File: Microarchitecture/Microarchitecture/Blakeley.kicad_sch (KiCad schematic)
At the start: 13 parts

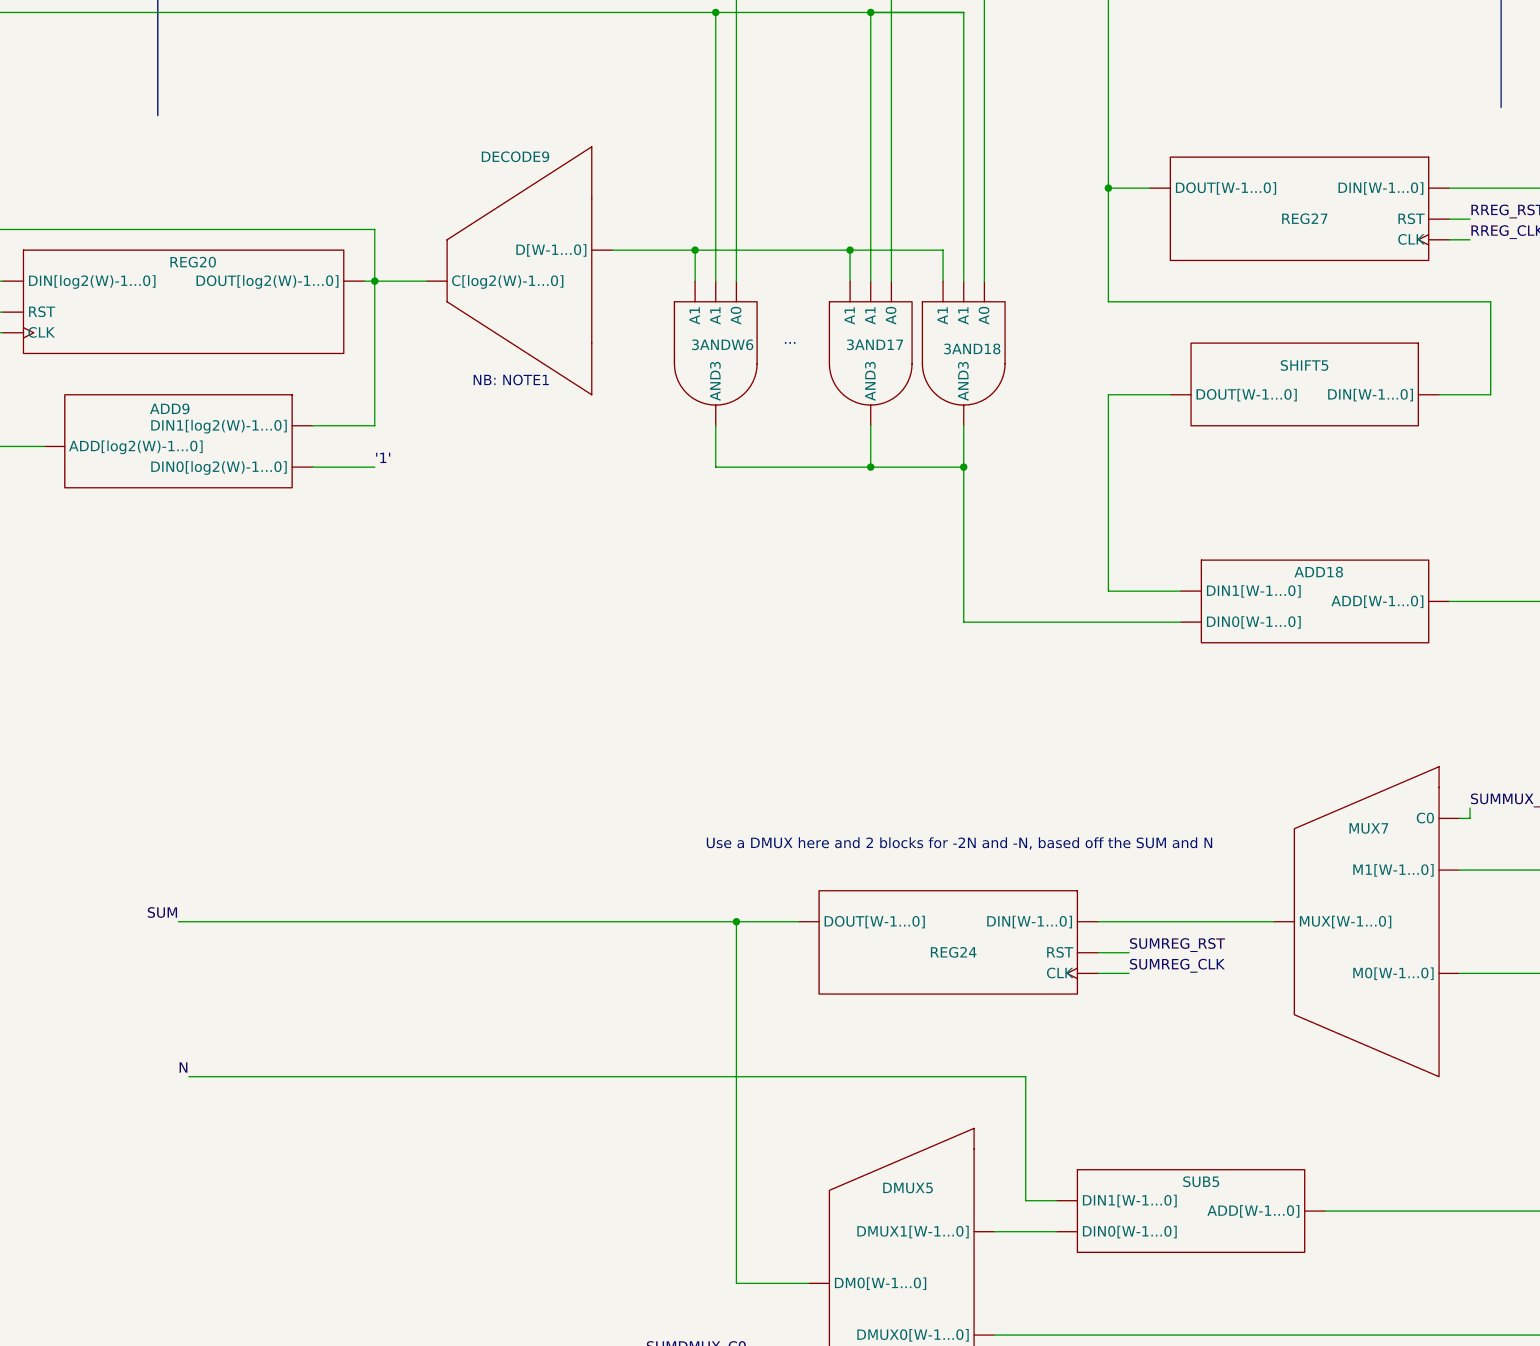
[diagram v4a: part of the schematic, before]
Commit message: Added comments, 16 to 8 stage pipeline
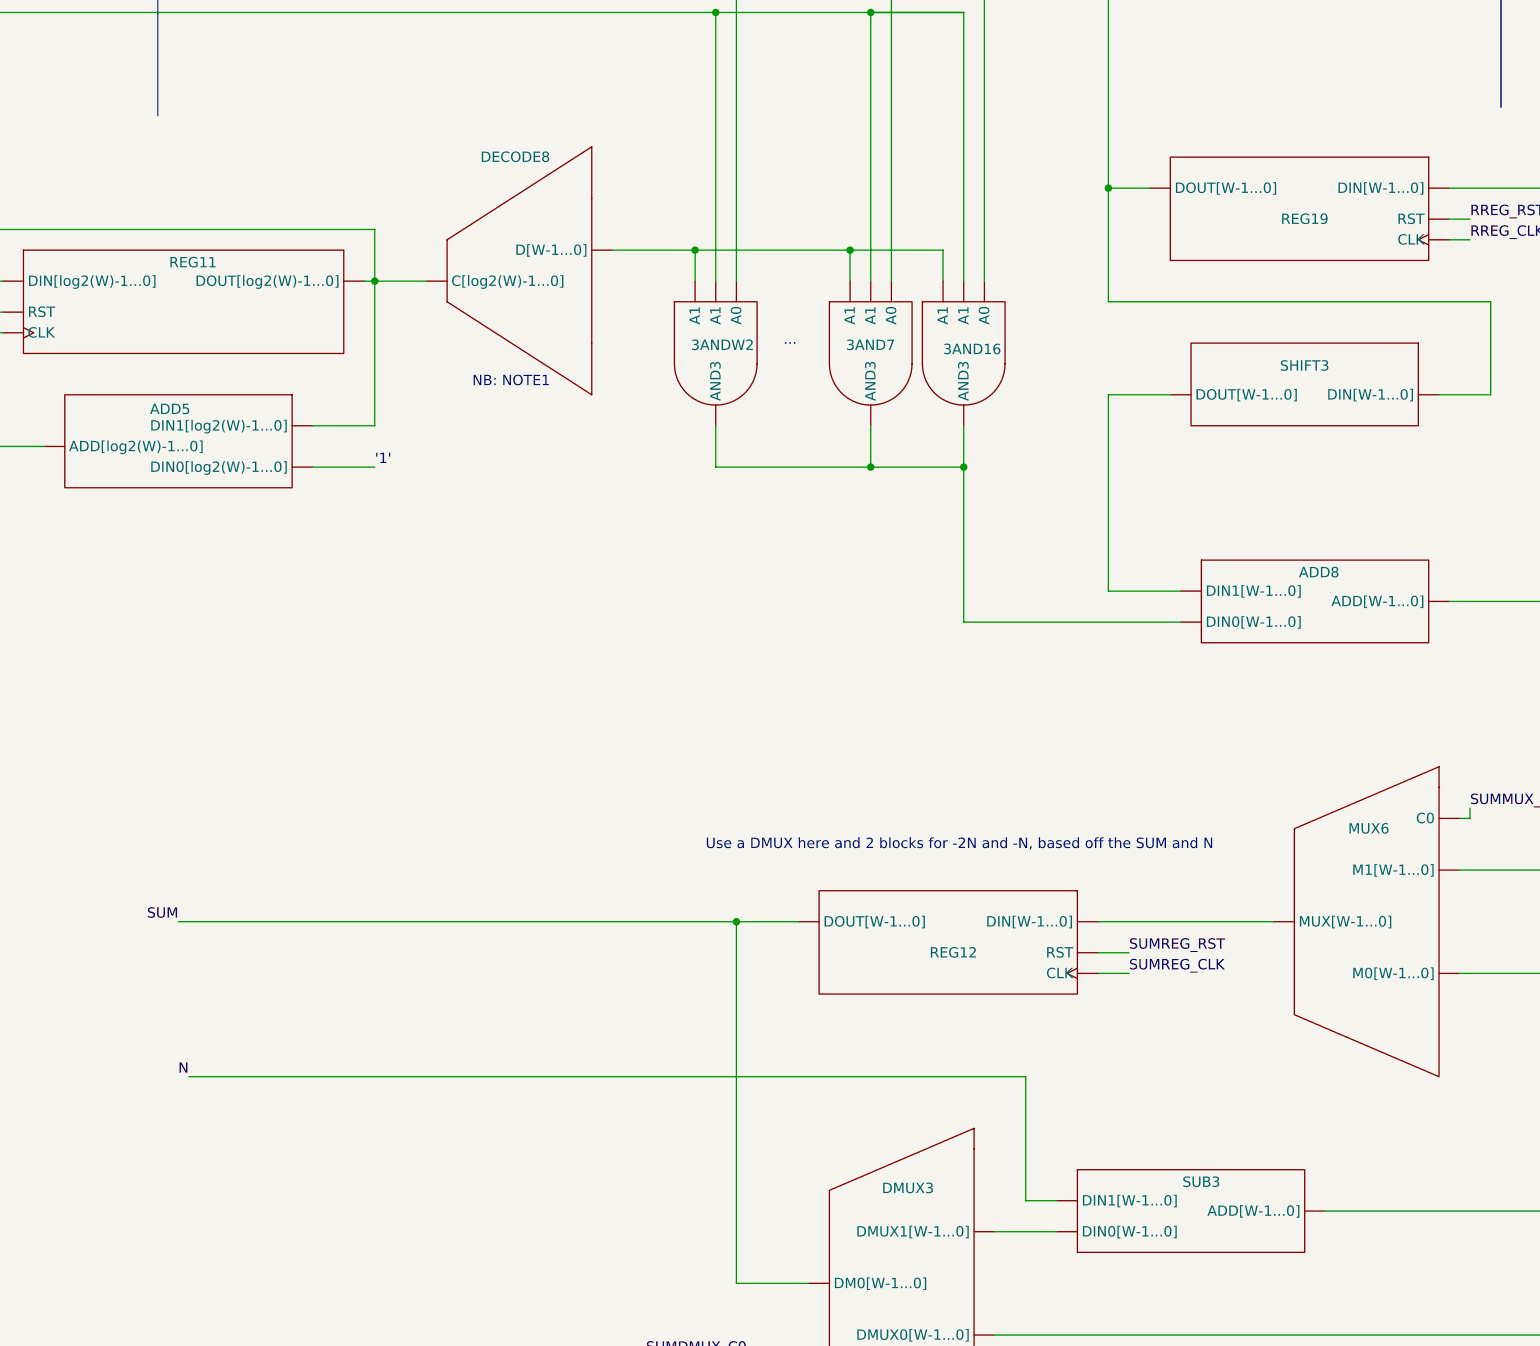
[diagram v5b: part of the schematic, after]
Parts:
- renumbered 3AND18 to 3AND16, 3AND17 to 3AND7, 3ANDW6 to 3ANDW2, ADD9 to ADD5, ADD18 to ADD8, DECODE9 to DECODE8, DMUX5 to DMUX3, MUX7 to MUX6, REG20 to REG11, REG24 to REG12, REG27 to REG19, SHIFT5 to SHIFT3, SUB5 to SUB3
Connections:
- net at ADD8. (DIN1[W-1...0]): now also MUX6. (MUX[W-1...0]); no longer SHIFT3. (DOUT[W-1...0])
- new net: ADD5. (DIN1[log2(W)-1...0]), REG11. (RST)
- new net: 3AND16. (AND3), 3AND7. (AND3), 3ANDW2. (AND3), DECODE8. (D[W-1...0])
- new net: 3AND16. (AND3), 3AND7. (AND3), 3ANDW2. (AND3), ADD8. (DIN1[W-1...0])
- new net: ADD8. (DIN1[W-1...0]), SHIFT3. (DOUT[W-1...0])
- new net: MUX6. (MUX[W-1...0]), SUB3. (DIN1[W-1...0])
- new net: MUX6. (MUX[W-1...0]), REG12. (RST)
- new net: DMUX3. (DMUX1[W-1...0]), REG19. (RST)
- new net: DMUX3. (DMUX1[W-1...0]), SUB3. (DIN1[W-1...0])

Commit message: Tried to update tb
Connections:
- net at ADD8. (DIN1[W-1...0]): now also MUX6. (MUX[W-1...0]); no longer SHIFT3. (DOUT[W-1...0])
- new net: ADD5. (DIN1[log2(W)-1...0]), REG11. (RST)
- new net: 3AND16. (AND3), 3AND7. (AND3), 3ANDW2. (AND3), DECODE8. (D[W-1...0])
- new net: 3AND16. (AND3), 3AND7. (AND3), 3ANDW2. (AND3), ADD8. (DIN1[W-1...0])
- new net: ADD8. (DIN1[W-1...0]), SHIFT3. (DOUT[W-1...0])
- new net: MUX6. (MUX[W-1...0]), SUB3. (DIN1[W-1...0])
- new net: MUX6. (MUX[W-1...0]), REG12. (RST)
- new net: DMUX3. (DMUX1[W-1...0]), REG19. (RST)
- new net: DMUX3. (DMUX1[W-1...0]), SUB3. (DIN1[W-1...0])
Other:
- moved on the sheet: SHIFT3
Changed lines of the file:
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@@
 		(dnp no)
 		(property "Reference" "SHIFT3"
-			(at 339.09 96.774 0)
+			(at 339.598 102.616 0)
 			(effects
 				(font
@@
 		)
 		(instances
-			(project "Microarchitecture"
+			(project ""
+				(path "/7e18b03f-0dd8-4430-9873-65919f4f0c9c/21c2d8ae-34c8-4eeb-a025-0344b2d7e18d"
+					(reference "SHIFT2")
+					(unit 1)
+				)
 				(path "/7e18b03f-0dd8-4430-9873-65919f4f0c9c/21c2d8ae-34c8-4eeb-a025-0344b2d7e18d/5c7540d9-7028-48a5-955b-0e835a2154cd/49cf7aed-c9dc-43e0-9dd4-664fc1390d76"
 					(reference "SHIFT3")
